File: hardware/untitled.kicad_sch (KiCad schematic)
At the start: 1 part, among them U1 F1C100s

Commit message: Basic schematic
Need to add passives
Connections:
- net CLK_eMMC: now reaches U1.59 (PC0/SPI0_CLK/SDC1_CLK)
- net CMD_eMMC: now reaches U1.60 (PC1/SPI0_CS/SDC1_CMD)
- net D0_eMMC: now reaches U1.61 (PC2/SPI0_MISO/SDC1_D0)
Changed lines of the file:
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@@
+	(wire
+		(pts
+			(xy 52.07 44.45) (xy 62.23 44.45)
+		)
+		(stroke
+			(width 0)
+			(type default)
+		)
+	)
 	(wire
 		(pts
 			(xy 171.45 90.17) (xy 186.69 90.17)
+		)
+		(stroke
+			(width 0)
+			(type default)
+		)
+	)
+	(wire
+		(pts
+			(xy 52.07 46.99) (xy 62.23 46.99)
 		)
 		(stroke
@@
 	(wire
 		(pts
+			(xy 52.07 41.91) (xy 62.23 41.91)
+		)
+		(stroke
+			(width 0)
+			(type default)
+		)
+	)
+	(wire
+		(pts
 			(xy 171.45 85.09) (xy 186.69 85.09)
 		)
@@
 		(shape input)
 		(at 30.48 31.75 180)
+		(effects
+			(font
+				(size 1.27 1.27)
+			)
+			(justify right)
+		)
+	)
+	(hierarchical_label "D0_eMMC"
+		(shape input)
+		(at 52.07 46.99 180)
 		(effects
 			(font
@@
 		)
 	)
+	(hierarchical_label "CLK_eMMC"
+		(shape input)
+		(at 52.07 41.91 180)
+		(effects
+			(font
+				(size 1.27 1.27)
+			)
+			(justify right)
+		)
+	)
 	(hierarchical_label "CMD"
 		(shape input)
@@
 		)
 	)
+	(hierarchical_label "CMD_eMMC"
+		(shape input)
+		(at 52.07 44.45 180)
+		(effects
+			(font
+				(size 1.27 1.27)
+			)
+			(justify right)
+		)
+	)

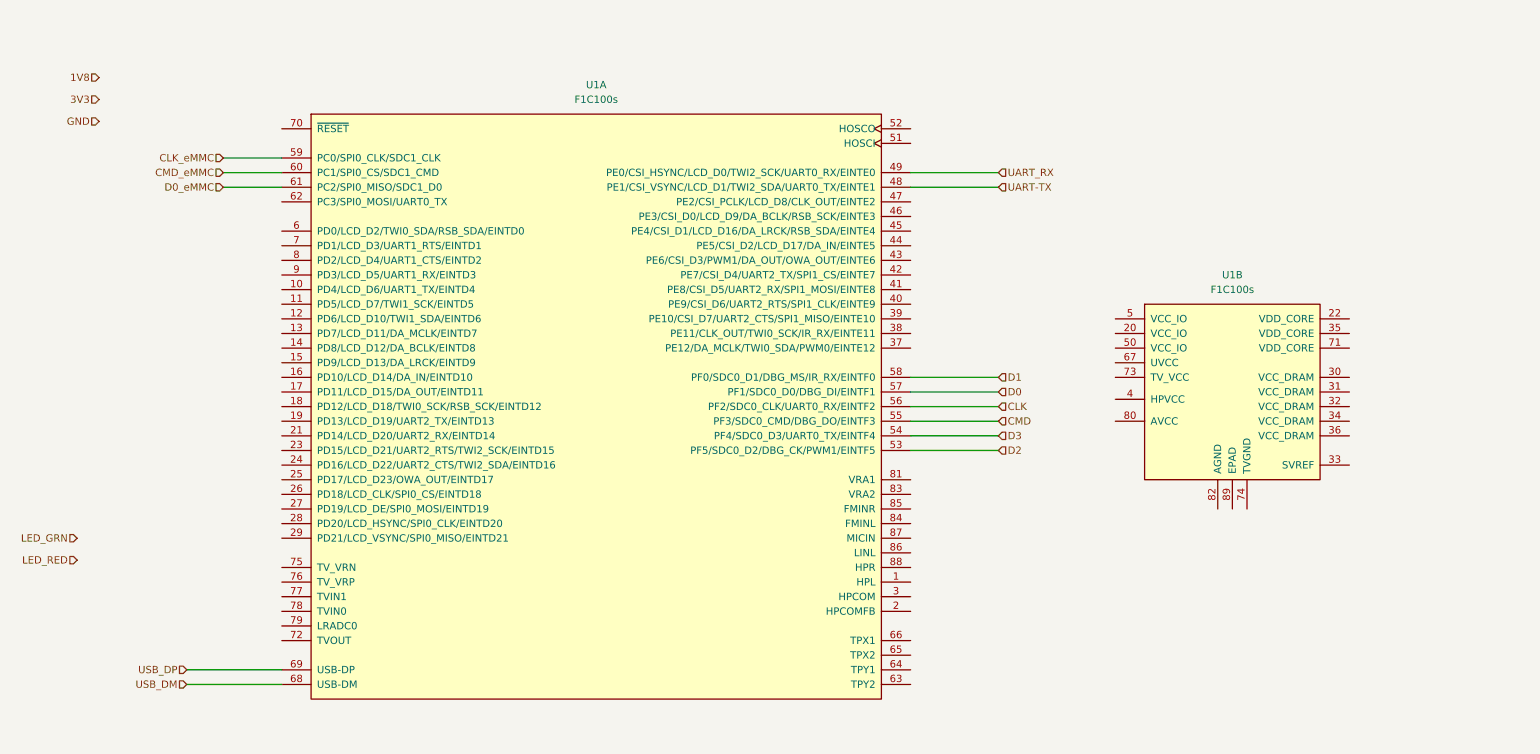
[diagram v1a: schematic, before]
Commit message: added data/clk resistors (33ohm)
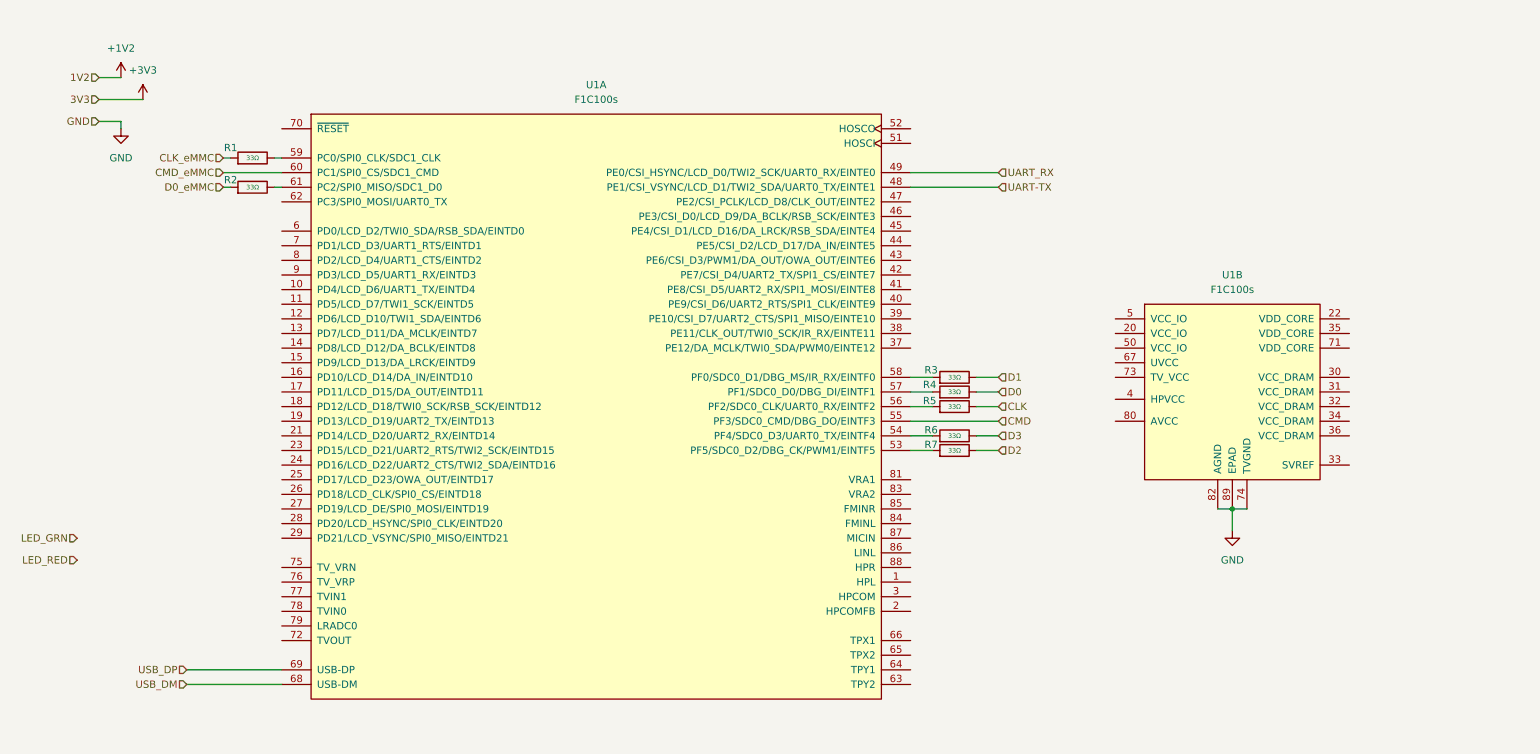
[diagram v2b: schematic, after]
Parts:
- added R1, R2, R3, R4, R5, R6, R7: 33Ω, PCM_JLCPCB:R_0402, symbol PCM_JLCPCB-Resistors:0402,33Ω
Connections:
- net CLK: now also R5.2; no longer U1.56 (PF2/SDC0_CLK/UART0_RX/EINTF2)
- net CLK_eMMC: now also R1.1; no longer U1.59 (PC0/SPI0_CLK/SDC1_CLK)
- net D0: now also R4.2; no longer U1.57 (PF1/SDC0_D0/DBG_DI/EINTF1)
- net D0_eMMC: now also R2.1; no longer U1.61 (PC2/SPI0_MISO/SDC1_D0)
- net D1: now also R3.2; no longer U1.58 (PF0/SDC0_D1/DBG_MS/IR_RX/EINTF0)
- net D2: now also R7.2; no longer U1.53 (PF5/SDC0_D2/DBG_CK/PWM1/EINTF5)
- net D3: now also R6.2; no longer U1.54 (PF4/SDC0_D3/UART0_TX/EINTF4)
- net GND: now also U1.74 (TVGND), U1.82 (AGND), U1.89 (EPAD)
- new net: R6.1, U1.54 (PF4/SDC0_D3/UART0_TX/EINTF4)
- new net: R7.1, U1.53 (PF5/SDC0_D2/DBG_CK/PWM1/EINTF5)
- new net: R5.1, U1.56 (PF2/SDC0_CLK/UART0_RX/EINTF2)
- new net: R4.1, U1.57 (PF1/SDC0_D0/DBG_DI/EINTF1)
- new net: R3.1, U1.58 (PF0/SDC0_D1/DBG_MS/IR_RX/EINTF0)
- new net: R1.2, U1.59 (PC0/SPI0_CLK/SDC1_CLK)
- new net: R2.2, U1.61 (PC2/SPI0_MISO/SDC1_D0)

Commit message: Added core decoupling caps
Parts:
- added C10, C11, C12, C13, C14, C15, C16, C18, C19, C20, C21, C22, C23, C24, C7, C9: 100nF, PCM_JLCPCB:C_0603, symbol PCM_JLCPCB-Capacitors:0603,100nF
- added C17, C25, C8: 1uF, PCM_JLCPCB:C_0402, symbol PCM_JLCPCB-Capacitors:0402,1uF
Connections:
- net +1V2: now also U1.22 (VDD_CORE), U1.35 (VDD_CORE), U1.71 (VDD_CORE), C10.1, C7.1, C8.1, C9.1
- net +3V3: now also U1.20 (VCC_IO), U1.30 (VCC_DRAM), U1.31 (VCC_DRAM), U1.32 (VCC_DRAM), U1.33 (SVREF), U1.34 (VCC_DRAM), U1.36 (VCC_DRAM), U1.4 (HPVCC), U1.5 (VCC_IO), U1.50 (VCC_IO), U1.67 (UVCC), U1.73 (TV_VCC), U1.80 (AVCC), C11.1, C12.1, C13.1, C14.1, C15.1, C16.1, C17.1, C18.1, C19.1, C20.1, C21.1, C22.1, C23.1, C24.1, C25.1
- net GND: now also C10.2, C11.2, C12.2, C13.2, C14.2, C15.2, C16.2, C17.2, C18.2, C19.2, C20.2, C21.2, C22.2, C23.2, C24.2, C25.2, C7.2, C8.2, C9.2
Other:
- moved on the sheet: R1, R2, R3, R4, R5, R6, R7, U1A

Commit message: Board design started
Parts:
- U1: footprint 3340:QFN-88_EP_10x10_Pitch0.4mm -> Package_DFN_QFN:ArtInChip_QFN-88-1EP_10x10mm_P0.4mm_EP6.74x6.74mm
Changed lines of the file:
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@@
 			)
 		)
-		(property "Footprint" "3340:QFN-88_EP_10x10_Pitch0.4mm"
+		(property "Footprint" "Package_DFN_QFN:ArtInChip_QFN-88-1EP_10x10mm_P0.4mm_EP6.74x6.74mm"
 			(at 43.18 49.53 0)
 			(effects
@@
 			)
 		)
-		(property "Footprint" "3340:QFN-88_EP_10x10_Pitch0.4mm"
+		(property "Footprint" "Package_DFN_QFN:ArtInChip_QFN-88-1EP_10x10mm_P0.4mm_EP6.74x6.74mm"
 			(at 173.99 38.1 0)
 			(effects

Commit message: PCB major changes
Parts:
- added R13, R14, R15, R16: 1kΩ, PCM_JLCPCB:R_0603, symbol PCM_JLCPCB-Resistors:0603,1kΩ
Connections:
- new net LED_1: R13.1
- new net LED_2: R14.1
- new net LED_3: R15.1
- new net LED_4: R16.1

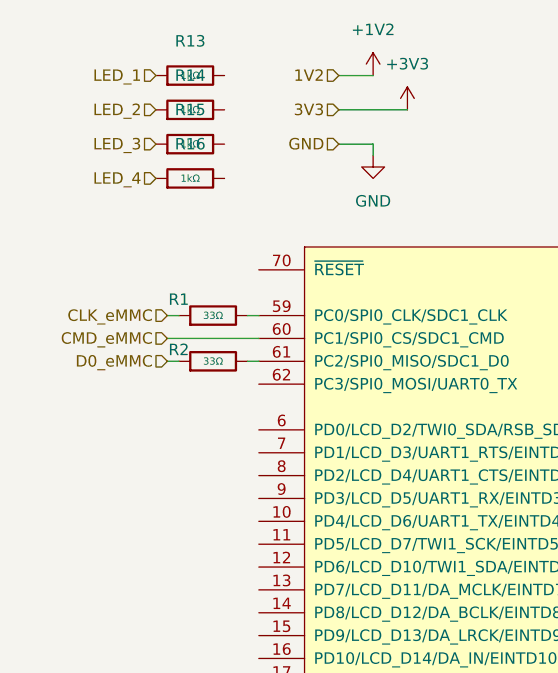
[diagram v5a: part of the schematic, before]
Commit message: Moved LEDs, renamed testpoints
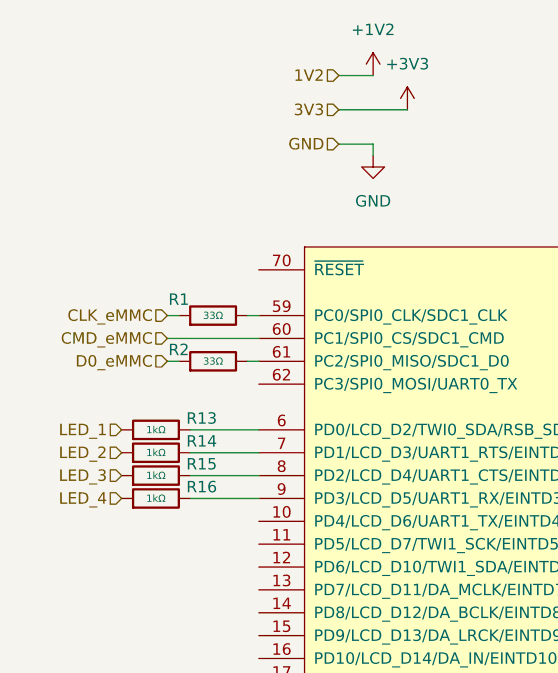
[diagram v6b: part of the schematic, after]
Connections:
- net at R14.2: now also U1.7 (PD1/LCD_D3/UART1_RTS/EINTD1)
- net at R15.2: now also U1.8 (PD2/LCD_D4/UART1_CTS/EINTD2)
- net at R13.2: now also U1.6 (PD0/LCD_D2/TWI0_SDA/RSB_SDA/EINTD0)
- net at U1.9 (PD3/LCD_D5/UART1_RX/EINTD3): now also R16.2
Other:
- moved on the sheet: R13, R14, R15, R16

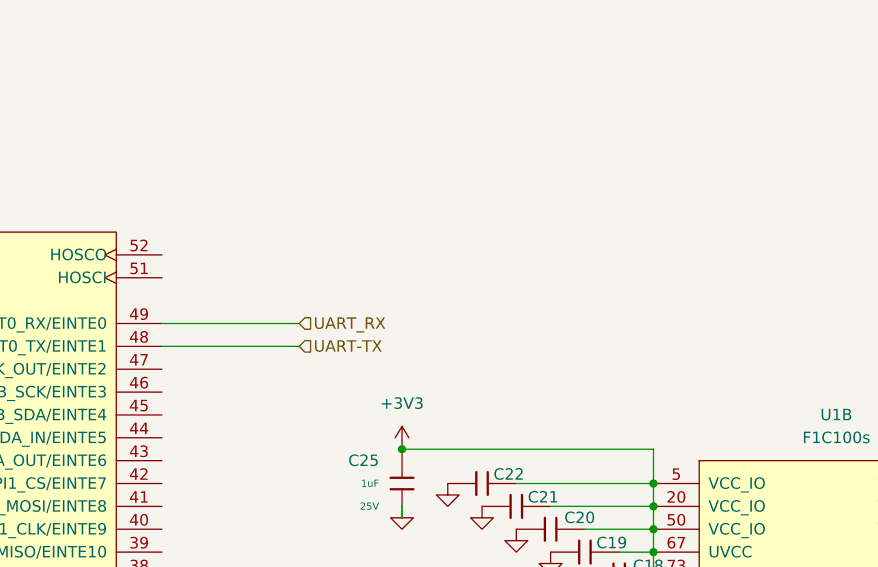
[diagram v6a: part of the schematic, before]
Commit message: added quartz
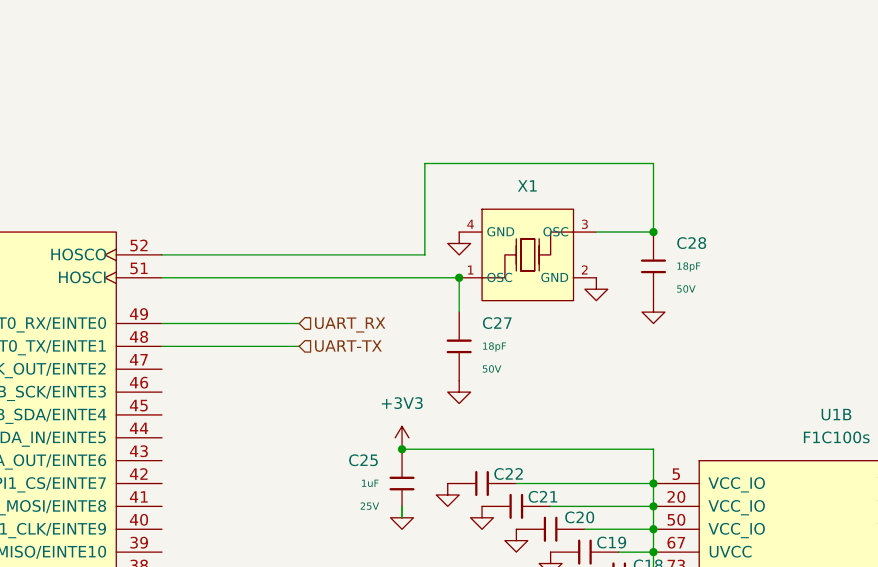
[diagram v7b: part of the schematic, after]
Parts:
- added C27, C28: 18pF, PCM_JLCPCB:C_0402, symbol PCM_JLCPCB-Capacitors:0402,18pF
- added X1: 24MHz, PCM_JLCPCB:OSC-SMD_4P-L3.2-W2.5-BL, symbol PCM_JLCPCB-Crystals:Crystal, 25MHz, 11pF
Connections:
- net GND: now also C27.2, C28.2, X1.2 (GND), X1.4 (GND)
- net at U1.51 (HOSCI): now also C27.1, X1.1 (OSC)
- net at U1.52 (HOSCO): now also C28.1, X1.3 (OSC)
